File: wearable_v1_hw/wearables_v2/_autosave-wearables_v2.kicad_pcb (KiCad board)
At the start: 2 copper layers, 40.2 x 40 mm, 41 parts, among them IC1 STM32WB05KZV6TR, IC2 TPS7A0228PDBVR, J1 217175-0001, J2 Conn_01x03, J3 Conn_01x04, Q1 PMOS, SW1 Reset, SW2 SW_Nidec_CAS-120A1, U1 DLF162500LT-5028A1, U2 2450AT18A100E, U3 BMI270, U5 MCP73831-2-MC, Y1 ABM10W-32.0000MHZ-8-B1U-T3, Y2 Crystal

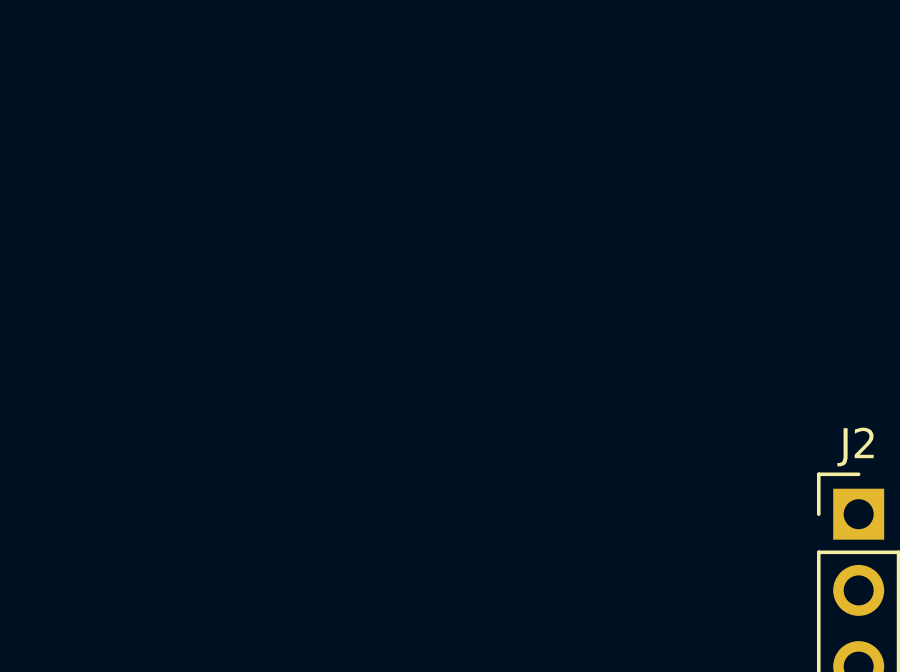
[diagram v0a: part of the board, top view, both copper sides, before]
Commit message: new nrf variant
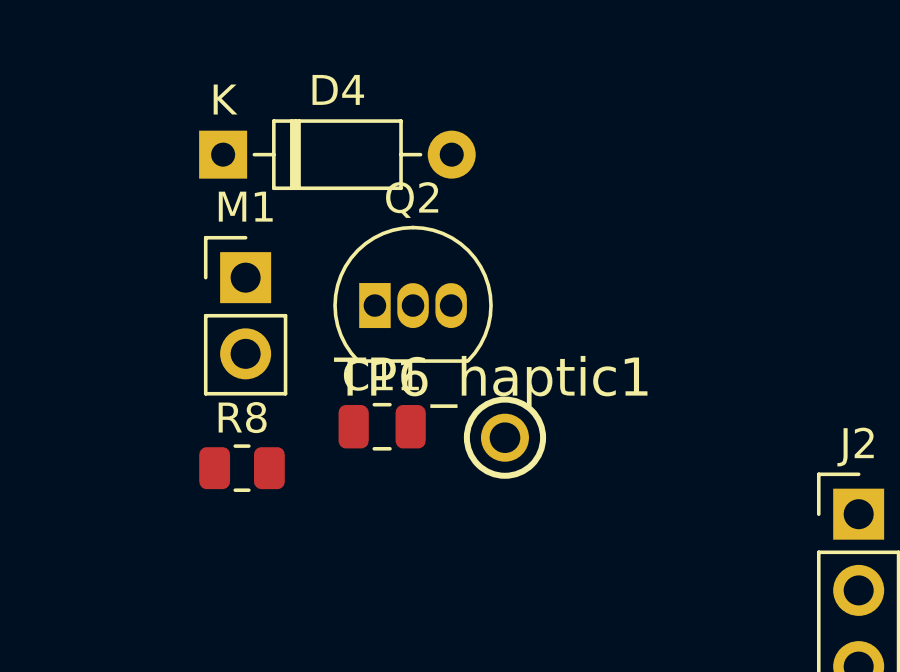
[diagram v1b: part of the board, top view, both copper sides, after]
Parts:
- added C11: 0.1uF, Capacitor_SMD:C_0805_2012Metric, F.Cu at (122.9, 66.1)
- added D4: 1N4148, Diode_THT:D_DO-35_SOD27_P7.62mm_Horizontal, F.Cu at (117.6, 57.0)
- added M1: Motor_DC, Connector_PinHeader_2.54mm:PinHeader_1x02_P2.54mm_Vertical, F.Cu at (118.4, 61.1)
- added Q2: S8050, Package_TO_SOT_THT:TO-92_Inline, F.Cu at (122.7, 62.1)
- added R8: 2k, Resistor_SMD:R_0805_2012Metric, F.Cu at (118.3, 67.5)
- added TP6_haptic1: TestPoint, A_wearables:5000, F.Cu at (127.0, 66.5)
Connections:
- IC1 pad 11: unconnected-(IC1-PA10-Pad11) -> /HAPTIC
- IC2 pad 1: Net-(IC2-EN) -> Net-(D1-K)
- IC2 pad 3: Net-(IC2-EN) -> Net-(D1-K)

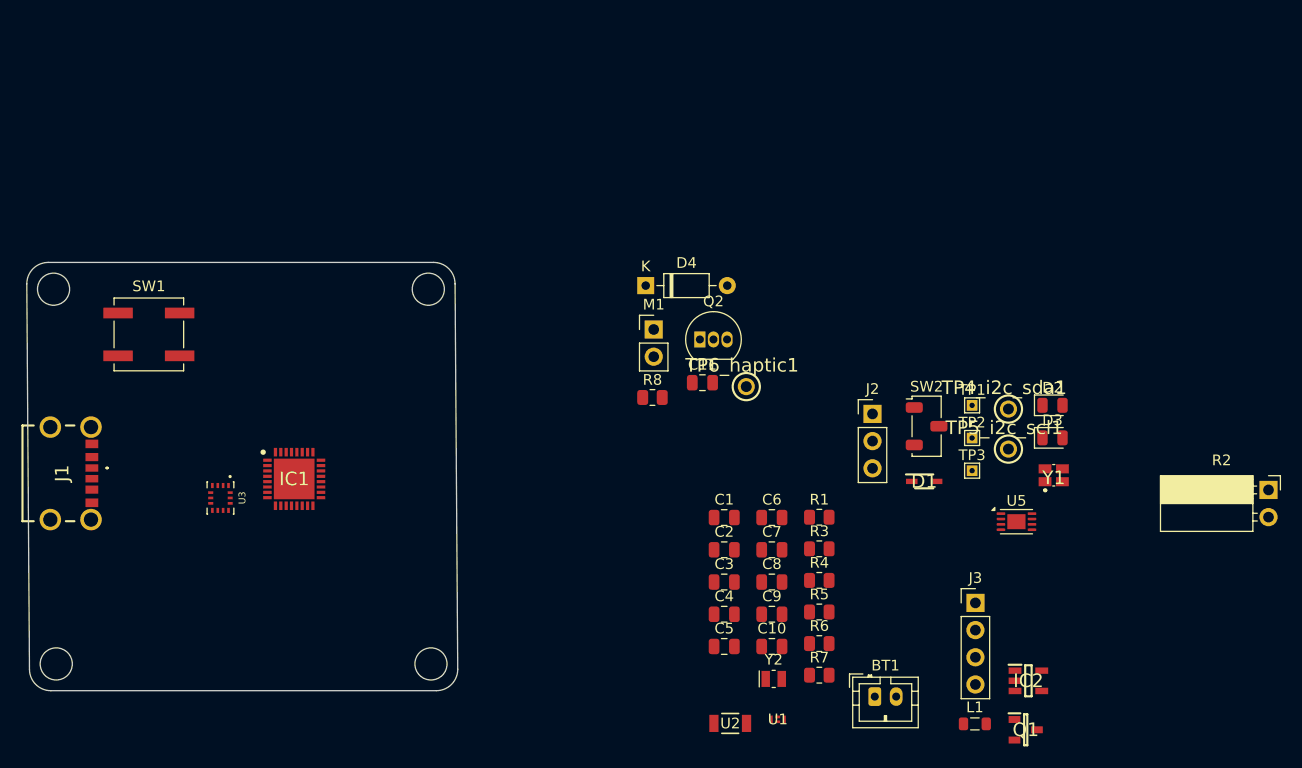
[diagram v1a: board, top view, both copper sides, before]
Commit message: finished nrf schematic/layout 👷‍♂️
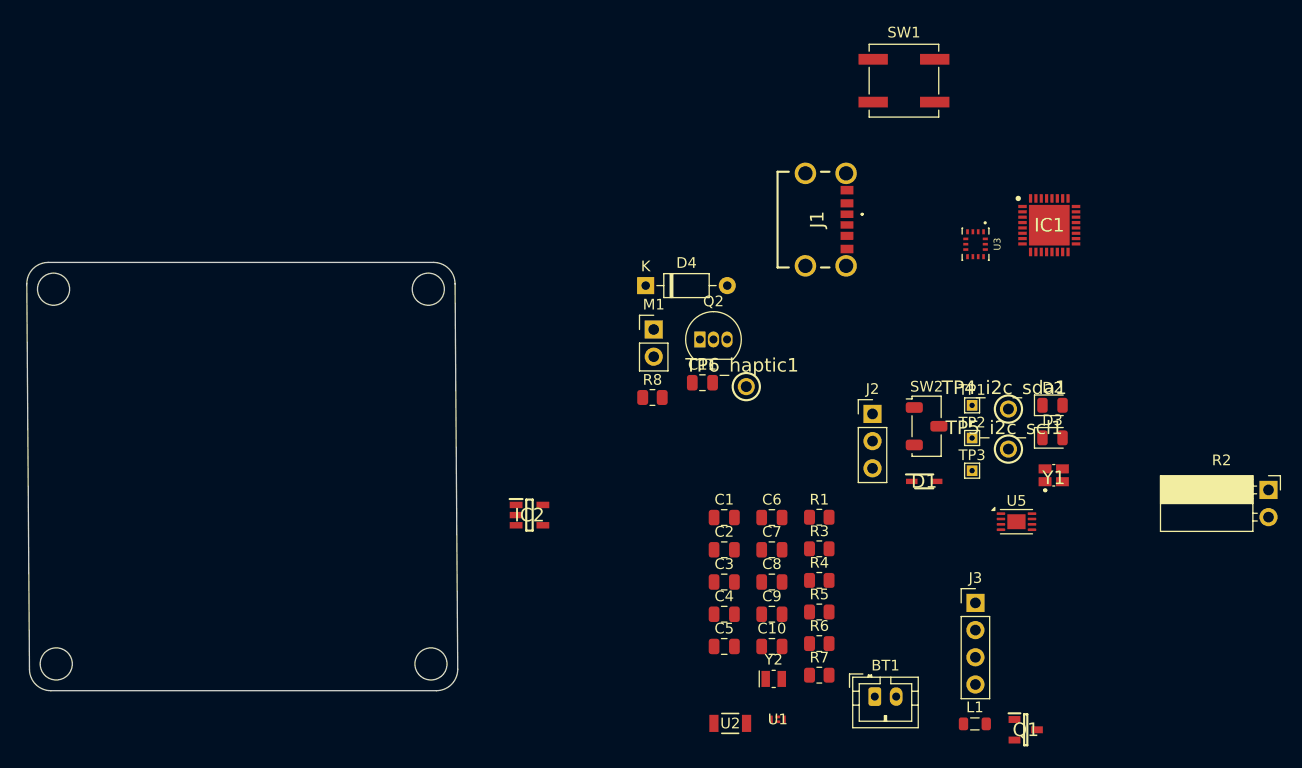
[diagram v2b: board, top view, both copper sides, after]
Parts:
- moved J1 74.4 mm to (133.4, 50.9)
- moved SW1 74.4 mm to (141.8, 37.9)
- moved U3 74.4 mm to (148.4, 53.2)
- moved IC1 74.4 mm to (155.3, 51.4)
- moved IC2 49.1 mm to (106.8, 78.5)
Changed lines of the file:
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@@
 	(footprint "Button_Switch_SMD:SW_SPST_B3SL-1002P"
 		(layer "F.Cu")
-		(at 71.225 61.6)
+		(at 141.75 37.9)
 		(descr "Middle Stroke Tactile Switch, B3SL")
 		(tags "Middle Stroke Tactile Switch")
@@
 	(footprint "A_wearables:2171750001"
 		(layer "F.Cu")
-		(at 62.8725 74.575 -90)
+		(at 133.3975 50.875 -90)
 		(descr "217175-0001")
 		(tags "Connector")
@@
 	(footprint "A_wearables:XDCR_BMI270"
 		(layer "F.Cu")
-		(at 77.9125 76.875 -90)
+		(at 148.4375 53.175 -90)
 		(property "Reference" "U3"
 			(at -0.008 -2.0314 90)
@@
 	(footprint "A_wearables:SOT95P280X145-5N"
 		(layer "F.Cu")
-		(at 153.375 93.95)
+		(at 106.775 78.475)
 		(descr "DBV0005A")
 		(tags "Integrated Circuit")
@@
 	(footprint "A_wearables:QFN50P500X500X100-33N-D"
 		(layer "F.Cu")
-		(at 84.8 75.1)
+		(at 155.325 51.4)
 		(descr "VFQFPN is a 32 lead, 5 x 5 mm, 0.50 mm pitch")
 		(tags "Integrated Circuit")
@@
 		(layer "F.Cu")
 		(pts
-			(xy 83.2 77.45) (xy 83.4 77.475)
+			(xy 153.725 53.75) (xy 153.925 53.775)
 		)
 		(height 7.353013)
 		(gr_text "0.2016 mm"
-			(at 82.611234 82.972632 352.8749837)
+			(at 153.136234 59.272632 352.8749837)
 			(layer "F.Cu")
 			(effects
@@
 		(layer "F.Cu")
 		(pts
-			(xy 87.925 71.975) (xy 81.675 71.975)
+			(xy 158.45 48.275) (xy 152.2 48.275)
 		)
 		(height 2.574999)
 		(gr_text "6.2500 mm"
-			(at 84.8 67.600001 0)
+			(at 155.325 43.900001 0)
 			(layer "F.Cu")
 			(effects
